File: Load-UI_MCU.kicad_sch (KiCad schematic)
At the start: 33 parts, among them IC1 MSPM0G3519SPMR, IC2 TPS73533DRVT, J1 Conn_01x05_Socket, J10 Conn_01x02_Socket, J11 Conn_01x02_Socket, J15 Conn_01x08_Pin, J8 Conn_01x06_Socket, SW1 SW_Push, SW2 SW_Push

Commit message: PCB finished, only final manufacturing files left, BOM, CPL
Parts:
- R8, R9: value 1k -> 4.7k
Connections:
- net SD_SCK: now also IC1.56 (PA10_/_CLK_OUT); no longer IC1.55 (PA9_/_RTC_OUT_/_CLK_OUT)
- net UART0_TX_XDS: now also IC1.35 (PA28); no longer IC1.56 (PA10_/_CLK_OUT)
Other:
- note added: "I2C2"
- note added: "SPI2"
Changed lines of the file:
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@@
 		)
 	)
-	(text "SPI1"
+	(text "SPI2\n"
 		(exclude_from_sim no)
 		(at 56.642 58.166 0)
@@
 		)
 	)
+	(text "I2C2"
+		(exclude_from_sim no)
+		(at 66.294 181.102 0)
+		(effects
+			(font
+				(size 1.27 1.27)
+			)
+		)
+	)
 	(text "Open Drain Pins"
 		(exclude_from_sim no)
@@
 	)
 	(no_connect
+		(at 146.05 40.64)
+	)
+	(no_connect
 		(at 181.61 109.22)
 	)
@@
 	)
 	(no_connect
-		(at 181.61 114.3)
-	)
-	(no_connect
 		(at 105.41 83.82)
 	)
@@
 	(wire
 		(pts
+			(xy 186.69 109.22) (xy 184.15 109.22)
+		)
+		(stroke
+			(width 0)
+			(type default)
+		)
+	)
+	(wire
+		(pts
 			(xy 234.95 46.99) (xy 231.14 46.99)
 		)
@@
 	(wire
 		(pts
+			(xy 143.51 38.1) (xy 147.32 38.1)
+		)
+		(stroke
+			(width 0)
+			(type default)
+		)
+	)
+	(wire
+		(pts
 			(xy 30.48 57.15) (xy 27.94 57.15)
 		)
@@
 	(wire
 		(pts
-			(xy 148.59 157.48) (xy 148.59 158.75)
+			(xy 181.61 114.3) (xy 184.15 114.3)
 		)
 		(stroke
@@
 	(wire
 		(pts
-			(xy 231.14 48.26) (xy 231.14 49.53)
+			(xy 148.59 157.48) (xy 148.59 158.75)
 		)
 		(stroke
@@
 	(wire
 		(pts
-			(xy 181.61 132.08) (xy 181.61 134.62)
+			(xy 231.14 48.26) (xy 231.14 49.53)
 		)
 		(stroke
@@
 	(wire
 		(pts
-			(xy 146.05 38.1) (xy 146.05 40.64)
+			(xy 181.61 132.08) (xy 181.61 134.62)
 		)
 		(stroke
@@
 		)
 	)
-	(wire
-		(pts
-			(xy 143.51 34.29) (xy 143.51 40.64)
-		)
-		(stroke
-			(width 0)
-			(type default)
-		)
-	)
 	(polyline
 		(pts
@@
 		)
 	)
+	(wire
+		(pts
+			(xy 184.15 109.22) (xy 184.15 114.3)
+		)
+		(stroke
+			(width 0)
+			(type default)
+		)
+	)
 	(polyline
 		(pts
@@
 		)
 	)
-	(wire
-		(pts
-			(xy 147.32 38.1) (xy 146.05 38.1)
-		)
-		(stroke
-			(width 0)
-			(type default)
-		)
-	)
 	(polyline
 		(pts
@@
 	(wire
 		(pts
+			(xy 143.51 38.1) (xy 143.51 40.64)
+		)
+		(stroke
+			(width 0)
+			(type default)
+		)
+	)
+	(wire
+		(pts
 			(xy 181.61 88.9) (xy 187.96 88.9)
 		)
@@
 	(global_label "UART0_TX_XDS"
 		(shape output)
-		(at 143.51 34.29 90)
+		(at 186.69 109.22 0)
 		(fields_autoplaced yes)
 		(effects
@@
 		)
 		(property "Intersheetrefs" "${INTERSHEET_REFS}"
-			(at 143.51 17.6373 90)
+			(at 203.3427 109.22 0)
 			(effects
 				(font
@@
 			)
 		)
-		(property "Value" "1k"
+		(property "Value" "4.7k"
 			(at 191.77 132.0799 0)
 			(effects
@@
 		(on_board yes)
 		(dnp no)
-		(fields_autoplaced yes)
 		(property "Reference" "R8"
 			(at 184.15 126.9999 0)
@@
 			)
 		)
-		(property "Value" "1k"
-			(at 184.15 129.5399 0)
+		(property "Value" "4.7k"
+			(at 183.642 129.54 0)
 			(effects
 				(font

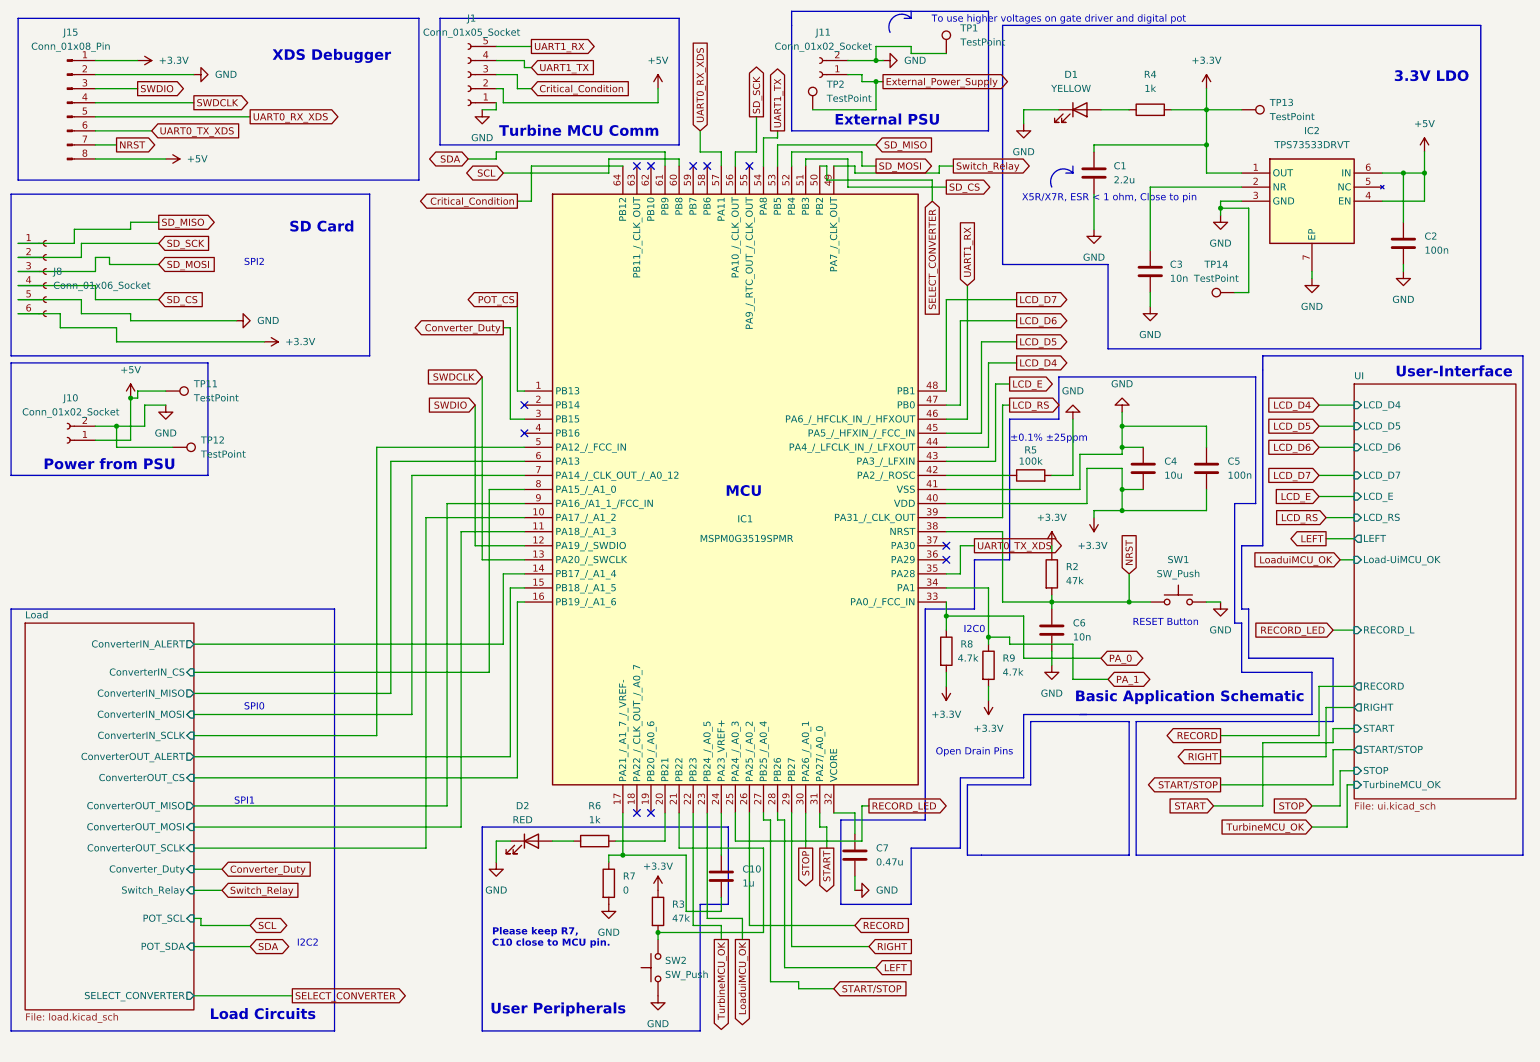
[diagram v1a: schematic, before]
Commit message: This commit contains all files up dote to Rev A. Load & UI MCU, manufactured on May 21, 2026
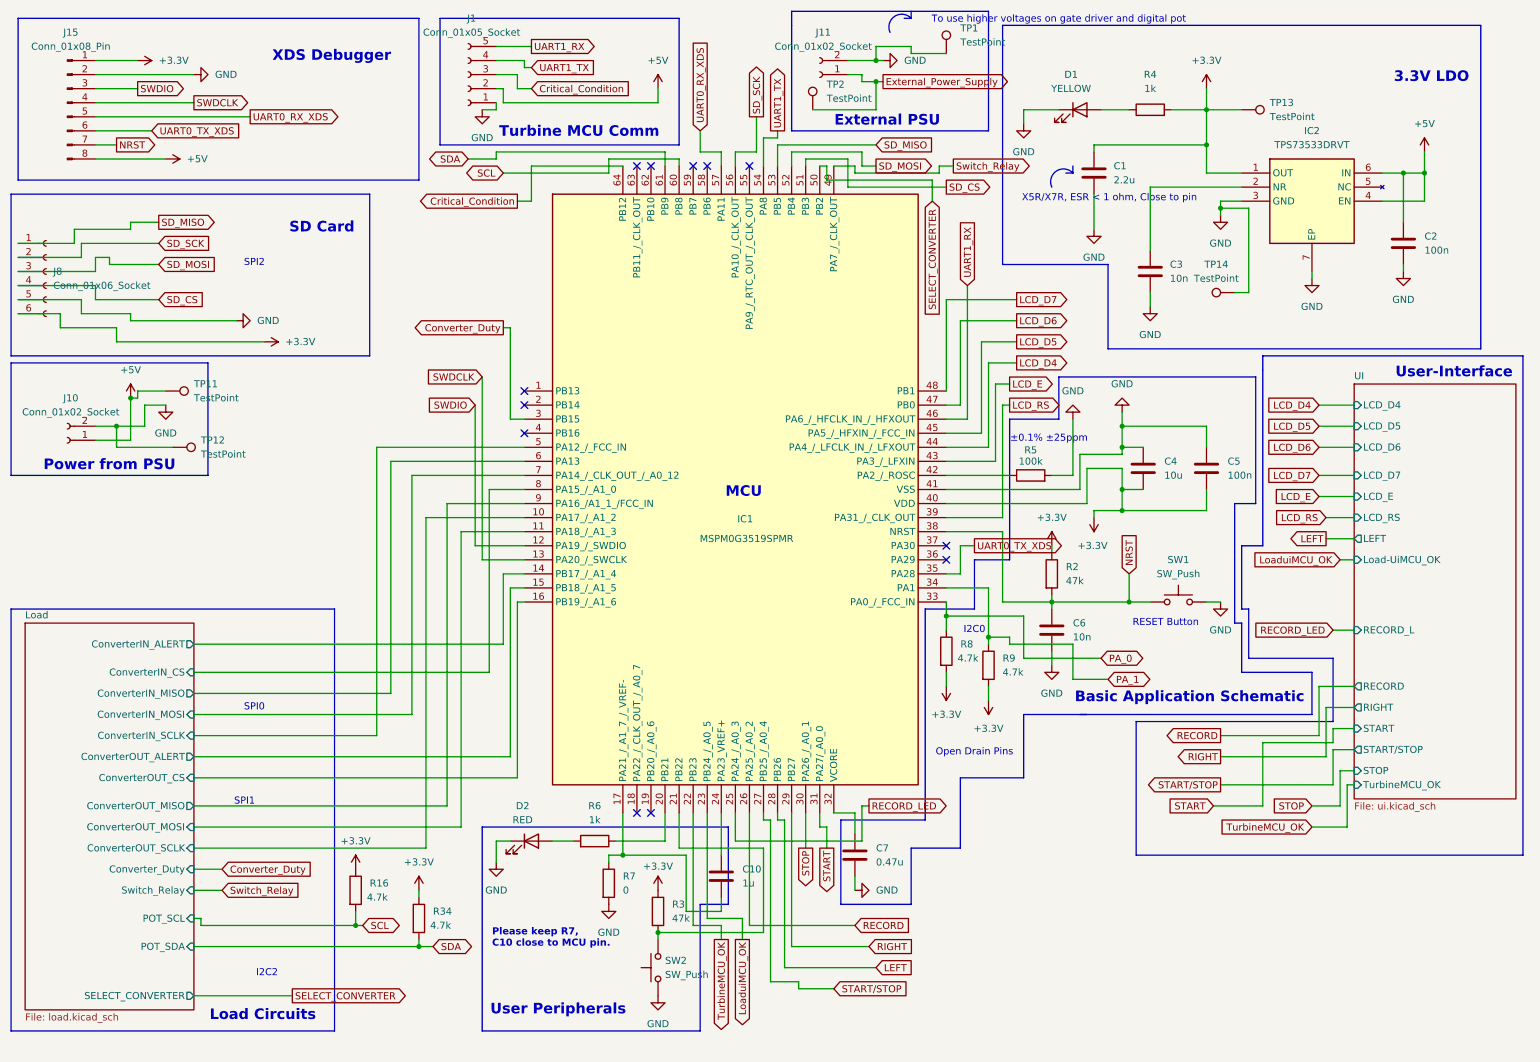
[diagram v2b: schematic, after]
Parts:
- added R16, R34: 4.7k, Resistor_SMD:R_0805_2012Metric_Pad1.20x1.40mm_HandSolder, symbol Device:R
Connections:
- net +3.3V: now also R16.1, R34.1
- net SCL: now also R16.2
- net SDA: now also R34.2
- net POT_CS: no longer names the net of IC1.1 (PB13)
- no-connect marks 11 -> 12
